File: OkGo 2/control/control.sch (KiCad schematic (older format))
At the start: 40 parts

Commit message: Removed RFM GPIOs, added control LCD, removed LEDs
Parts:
- removed P?: CONN_CH1, symbol CONN_01X05
- removed P?: CONN_CH2, symbol CONN_01X05
- removed P?: CONN_CH3, symbol CONN_01X05
- removed P?: CONN_CH4, symbol CONN_01X05
- removed R? (x8): R, symbol R
- added P?: CONN_CH1, symbol CONN_01X02
- added P?: CONN_CH2, symbol CONN_01X02
- added P?: CONN_CH3, symbol CONN_01X02
- added P?: CONN_CH4, symbol CONN_01X02
- added RV?: 20k LIN, symbol POT
- added U?: LCD_HD44780, symbol LCD_HD44780
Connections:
- net labels added: LCD_DB0, LCD_DB1, LCD_DB2, LCD_DB3, LCD_DB4, LCD_DB5, LCD_DB6, LCD_DB7, LCD_E, LCD_R/W, LCD_RS
- net labels removed: CH1_GRN, CH1_RED, CH2_GRN, CH2_RED, CH3_GRN, CH3_RED, CH4_GRN, CH4_RED, DIO0, DIO1, DIO2, DIO3, DIO4, DIO5
- wire segments 192 -> 170
- no-connect marks 2 -> 8
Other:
- moved on the sheet: C?, P?, R?, U?

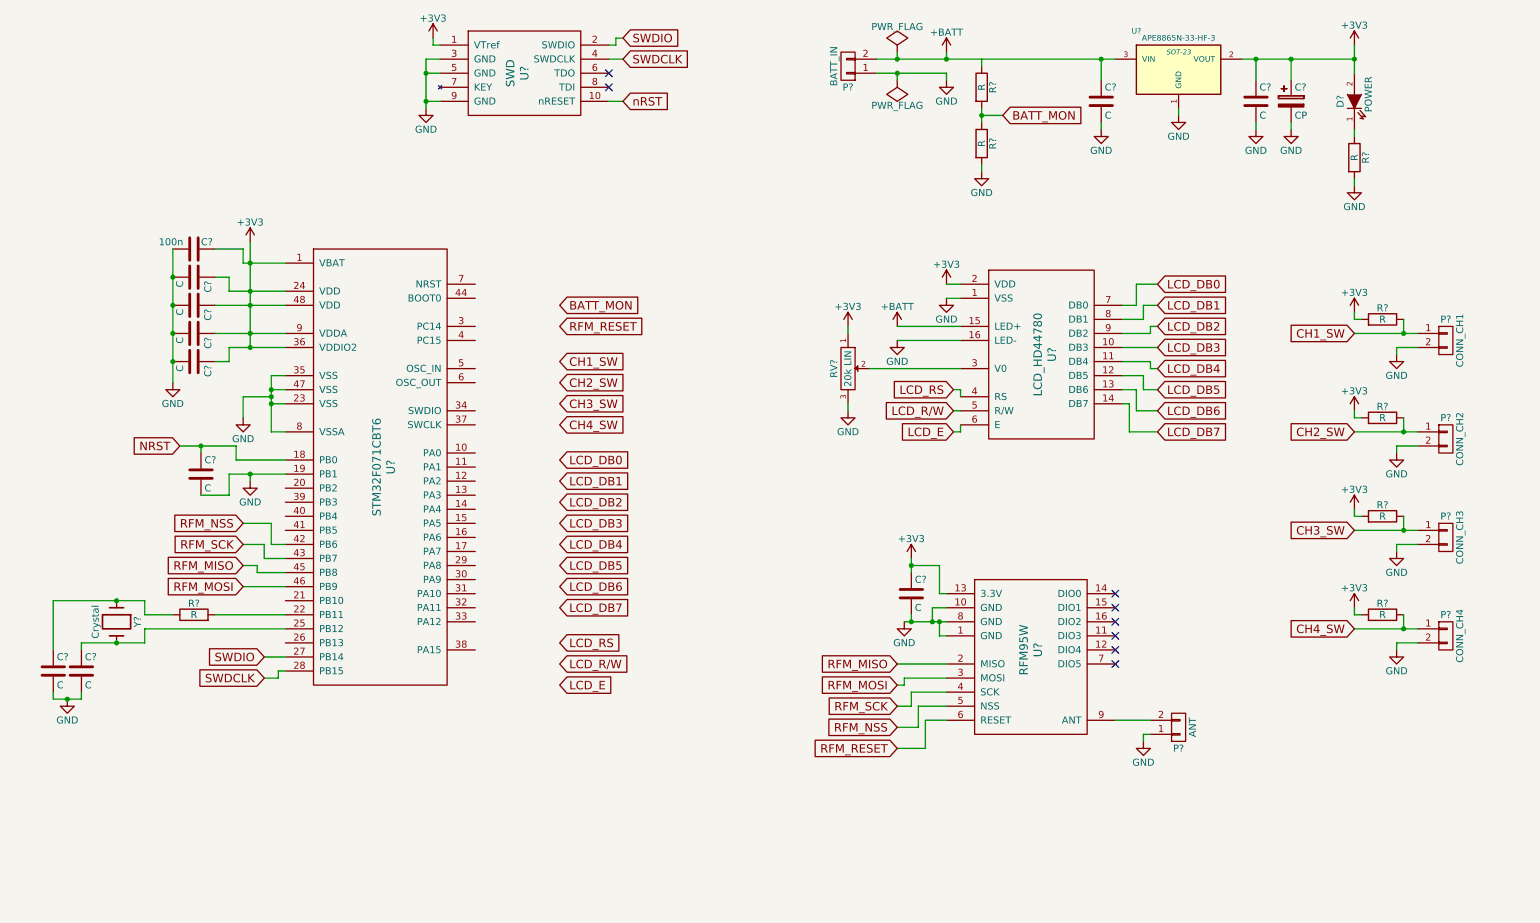
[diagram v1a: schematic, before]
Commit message: Updated schematics to new KiCAD
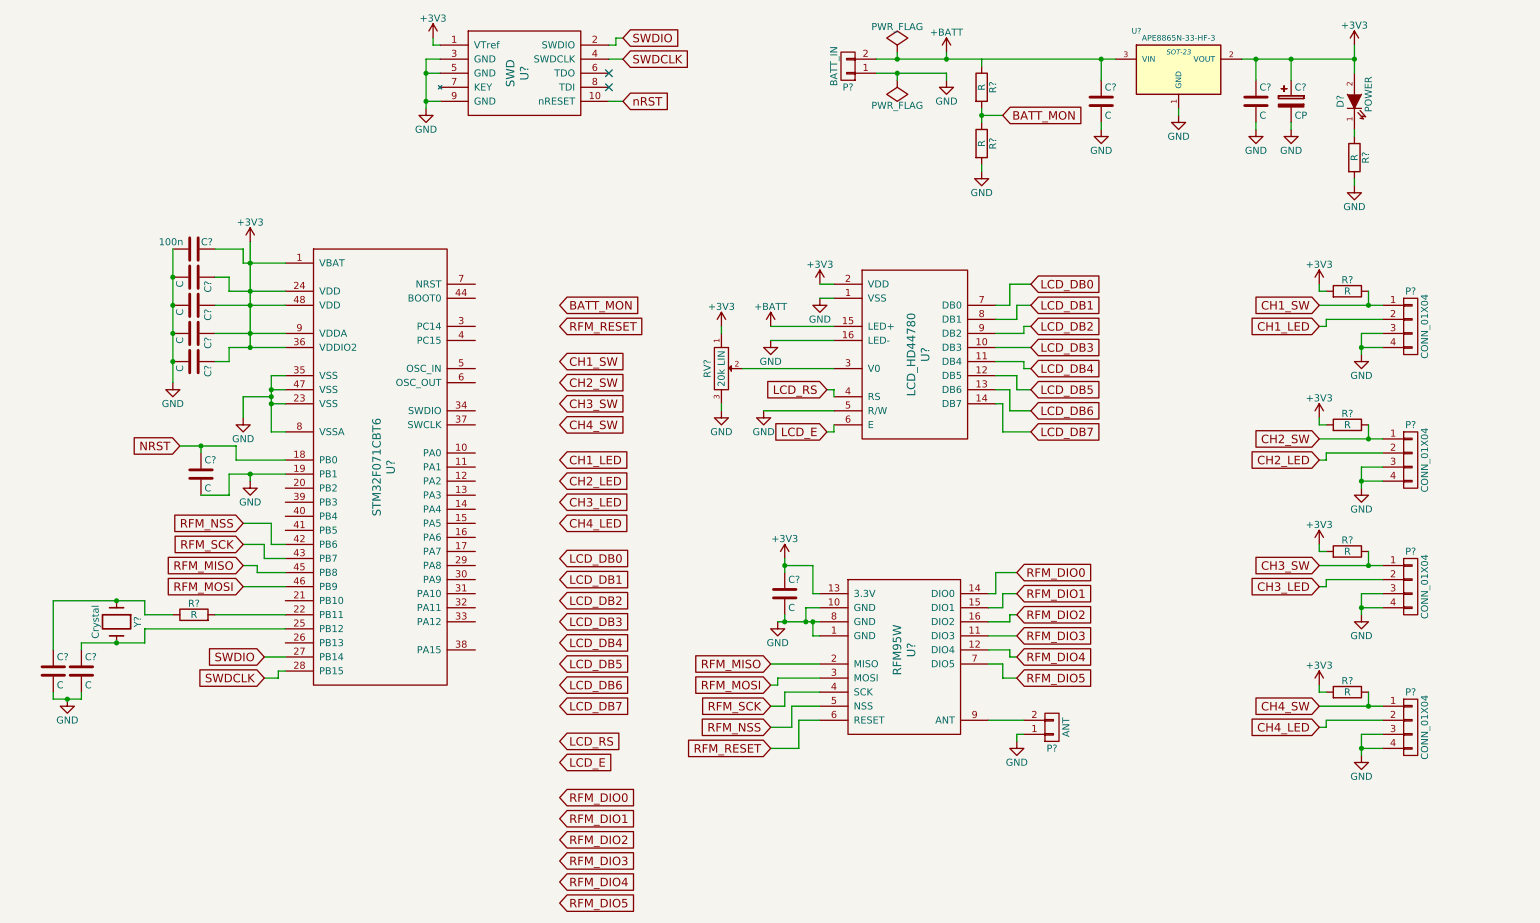
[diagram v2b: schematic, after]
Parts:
- removed P?: CONN_CH1, symbol CONN_01X02
- removed P?: CONN_CH2, symbol CONN_01X02
- removed P?: CONN_CH3, symbol CONN_01X02
- removed P?: CONN_CH4, symbol CONN_01X02
- added P? (x4): CONN_01X04, symbol CONN_01X04
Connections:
- net LCD_R/W is gone; now on net GND: U?.5 (R/W)
- net CH1_SW: now also P?.1 (P1)
- net CH2_SW: now also P?.1 (P1)
- net CH3_SW: now also P?.1 (P1)
- net CH4_SW: now also P?.1 (P1)
- net GND: now also P?.3 (P3), P?.3 (P3), P?.3 (P3), P?.3 (P3), P?.4 (P4), P?.4 (P4), P?.4 (P4), P?.4 (P4)
- net RFM_DIO3: now reaches U?.11 (DIO3)
- net RFM_DIO4: now reaches U?.12 (DIO4)
- net RFM_DIO0: now reaches U?.14 (DIO0)
- net RFM_DIO1: now reaches U?.15 (DIO1)
- net RFM_DIO2: now reaches U?.16 (DIO2)
- net RFM_DIO5: now reaches U?.7 (DIO5)
- new net CH1_LED: P?.2 (P2)
- new net CH2_LED: P?.2 (P2)
- new net CH3_LED: P?.2 (P2)
- new net CH4_LED: P?.2 (P2)
- no-connect marks 8 -> 2
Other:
- moved on the sheet: C?, P?, R?, RV?, U?

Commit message: Removed SPI pins from STM32 pinout.
Made them generic pins for more flexibility and less weirdness.  Resolves #1.
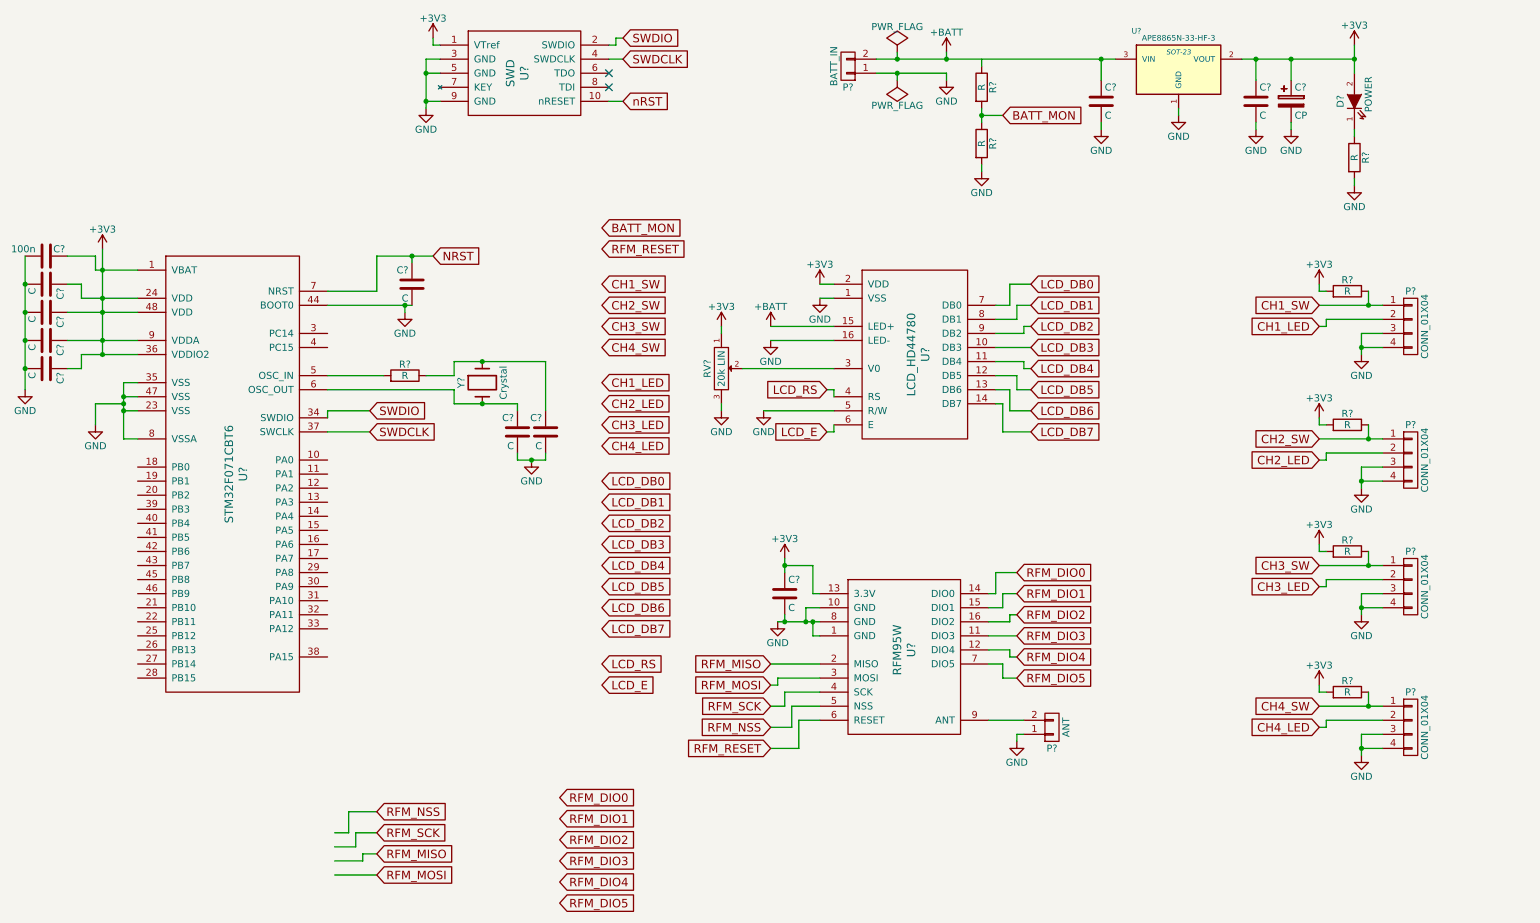
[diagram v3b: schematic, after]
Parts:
- removed U?: STM32F071CBT6, symbol STM32F071CBT6
- added U?: STM32F071CBT6, symbol STM32F071CBT6
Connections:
- net +3V3: now also U?.1 (VBAT), U?.24 (VDD), U?.36 (VDDIO2), U?.48 (VDD), U?.9 (VDDA)
- net GND: now also U?.23 (VSS), U?.35 (VSS), U?.44 (BOOT0), U?.47 (VSS), U?.8 (VSSA)
- net NRST: now also U?.7 (NRST)
- net SWDCLK: now also U?.37 (SWCLK)
- net SWDIO: now also U?.34 (SWDIO)
- net at R?.2: now also U?.5 (OSC_IN)
- net at C?.1, Y?.2: now also U?.6 (OSC_OUT)
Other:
- moved on the sheet: C?, R?, Y?

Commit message: Added ESD suppression, resolves #13
Also removed redundant pulldowns on firing channels.
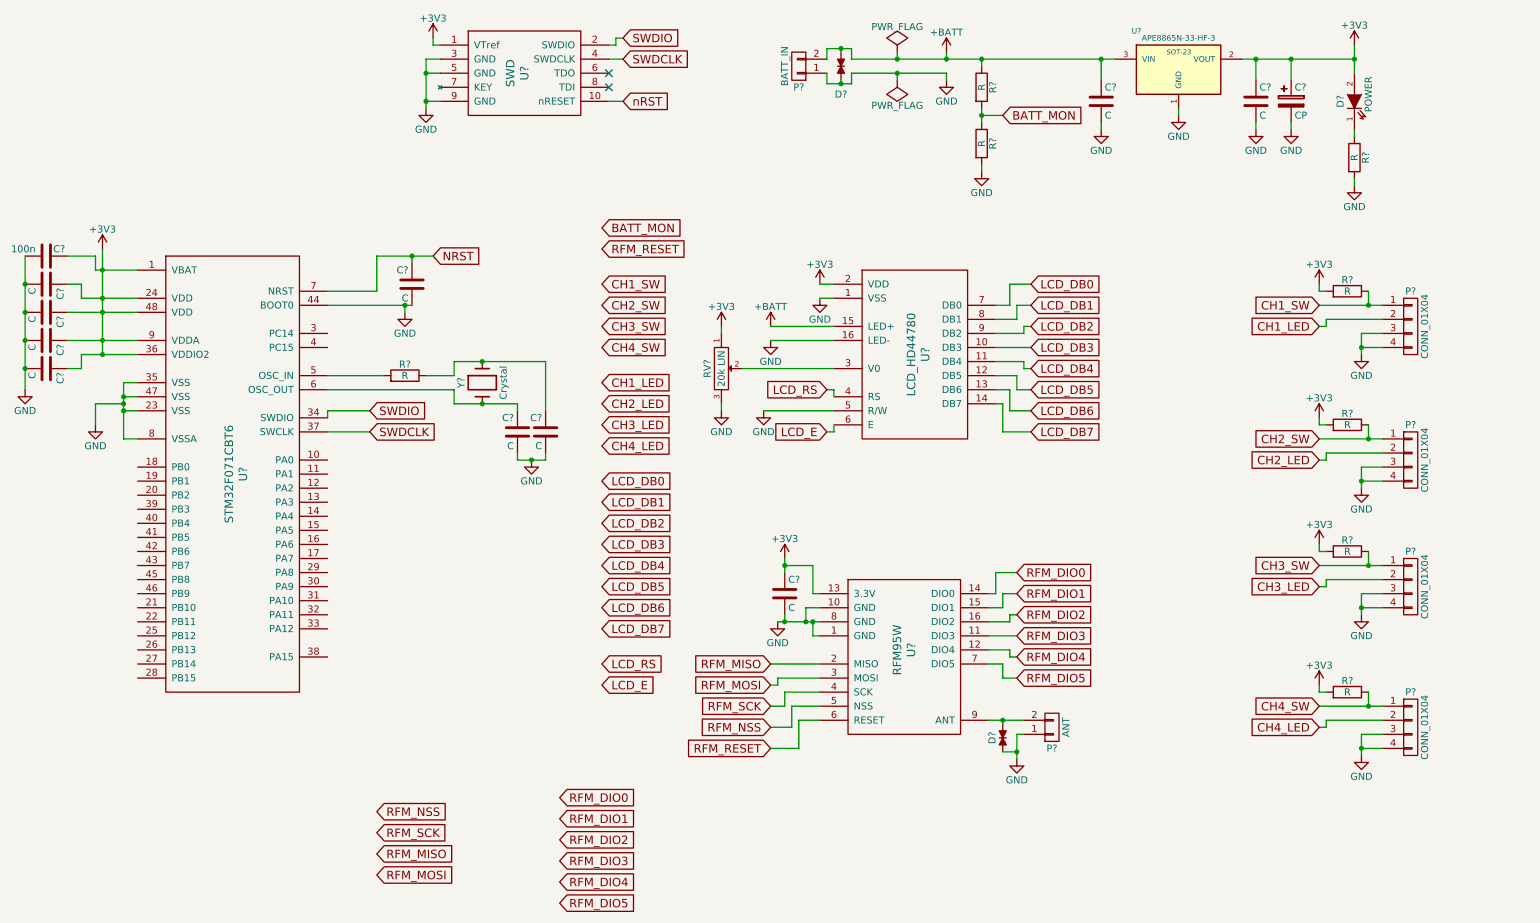
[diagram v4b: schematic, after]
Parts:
- added D? (x2): TVS_small, Resistors_SMD:R_0603_HandSoldering, symbol TVS_small
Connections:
- net +BATT: now also R?.1, D?.1
- net GND: now also D?.1, D?.2
- net at P?.2 (P2), U?.9 (ANT): now also D?.2
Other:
- moved on the sheet: P?
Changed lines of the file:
@@
 LIBS:lcd_hd44780
 LIBS:stm32f071cbt6
+LIBS:tvs_small
 LIBS:control-cache
 EELAYER 25 0
@@
 L CONN_01X02 P?
 U 1 1 556213DD
-P 6700 1150
-F 0 "P?" H 6700 1300 50  0000 C CNN
-F 1 "BATT_IN" V 6800 1150 50  0000 C CNN
-F 2 "" H 6700 1150 60  0000 C CNN
-F 3 "" H 6700 1150 60  0000 C CNN
-	1    6700 1150
+P 6350 1150
+F 0 "P?" H 6350 1300 50  0000 C CNN
+F 1 "BATT_IN" V 6450 1150 50  0000 C CNN
+F 2 "" H 6350 1150 60  0000 C CNN
+F 3 "" H 6350 1150 60  0000 C CNN
+	1    6350 1150
 	-1   0    0    1
 $EndComp
@@
 L GND #PWR?
 U 1 1 55629E65
-P 7900 5950
-F 0 "#PWR?" H 7900 5700 50  0001 C CNN
-F 1 "GND" H 7900 5800 50  0000 C CNN
-F 2 "" H 7900 5950 60  0000 C CNN
-F 3 "" H 7900 5950 60  0000 C CNN
-	1    7900 5950
+P 7900 6075
+F 0 "#PWR?" H 7900 5825 50  0001 C CNN
+F 1 "GND" H 7900 5925 50  0000 C CNN
+F 2 "" H 7900 6075 60  0000 C CNN
+F 3 "" H 7900 6075 60  0000 C CNN
+	1    7900 6075
 	1    0    0    -1
 $EndComp
@@
 	9850 1550 9850 1600
 Wire Wire Line
-	9500 1100 10300 1100
+	9500 1100 9600 1100
+Wire Wire Line
+	9600 1100 9850 1100
+Wire Wire Line
+	9850 1100 10300 1100
 Wire Wire Line
 	9600 1100 9600 1250
@@
 Connection ~ 9600 1100
 Wire Wire Line
-	10300 1000 10300 1200
+	10300 1000 10300 1100
+Wire Wire Line
+	10300 1100 10300 1200
 Connection ~ 9850 1100
 Wire Wire Line
-	6900 1200 7400 1200
+	6725 1200 7050 1200
+Wire Wire Line
+	7050 1200 7400 1200
 Wire Wire Line
 	7050 1050 7050 1100
@@
 	10350 3150 10500 3150
 Wire Wire Line
-	10350 3050 10350 3200
+	10350 3050 10350 3150
+Wire Wire Line
+	10350 3150 10350 3200
 Wire Wire Line
 	10350 4100 10500 4100
 Wire Wire Line
-	10350 4000 10350 4150
+	10350 4000 10350 4100
+Wire Wire Line
+	10350 4100 10350 4150
 Wire Wire Line
 	10350 5000 10500 5000
 Wire Wire Line
-	10350 4900 10350 5050
+	10350 4900 10350 5000
+Wire Wire Line
+	10350 5000 10350 5050
 Wire Wire Line
 	10350 6000 10500 6000
 Wire Wire Line
-	10350 5900 10350 6050
+	10350 5900 10350 6000
+Wire Wire Line
+	10350 6000 10350 6050
 Wire Wire Line
 	10400 2850 10400 2750
@@
 	10050 2750 10050 2700
 Wire Wire Line
-	10050 2850 10500 2850
-Wire Wire Line
-	10050 3800 10500 3800
+	10050 2850 10400 2850
+Wire Wire Line
+	10400 2850 10500 2850
+Wire Wire Line
+	10050 3800 10400 3800
+Wire Wire Line
+	10400 3800 10500 3800
 Wire Wire Line
 	10400 3800 10400 3700
@@
 	10050 3700 10050 3650
 Wire Wire Line
-	10050 4700 10500 4700
+	10050 4700 10400 4700
+Wire Wire Line
+	10400 4700 10500 4700
 Wire Wire Line
 	10100 4600 10050 4600
@@
 Connection ~ 10400 4700
 Wire Wire Line
-	10050 5700 10500 5700
+	10050 5700 10400 5700
+Wire Wire Line
+	10400 5700 10500 5700
 Wire Wire Line
 	10400 5600 10400 5700
@@
 	7950 5900 7900 5900
 Wire Wire Line
-	7900 5900 7900 5950
-Wire Wire Line
-	6200 5100 6500 5100
+	7900 5900 7900 6025
+Wire Wire Line
+	7900 6025 7900 6075
+Wire Wire Line
+	6200 5100 6250 5100
+Wire Wire Line
+	6250 5100 6400 5100
+Wire Wire Line
+	6400 5100 6450 5100
+Wire Wire Line
+	6450 5100 6500 5100
 Wire Wire Line
 	6450 5100 6450 5200
@@
 Connection ~ 6400 5100
 Wire Wire Line
-	6250 4650 6250 4750
+	6250 4650 6250 4700
+Wire Wire Line
+	6250 4700 6250 4750
 Wire Wire Line
 	6250 4700 6450 4700
@@
 Connection ~ 6250 5100
 Wire Wire Line
-	7950 5800 7700 5800
-Wire Wire Line
-	1400 2450 1400 3200
-Wire Wire Line
-	1250 2800 1650 2800
-Wire Wire Line
-	1150 2900 1650 2900
+	7950 5800 7800 5800
+Wire Wire Line
+	7800 5800 7700 5800
+Wire Wire Line
+	1400 2450 1400 2600
+Wire Wire Line
+	1400 2600 1400 2800
+Wire Wire Line
+	1400 2800 1400 2900
+Wire Wire Line
+	1400 2900 1400 3100
+Wire Wire Line
+	1400 3100 1400 3200
+Wire Wire Line
+	1250 2800 1400 2800
+Wire Wire Line
+	1400 2800 1650 2800
+Wire Wire Line
+	1150 2900 1400 2900
+Wire Wire Line
+	1400 2900 1650 2900
 Connection ~ 1400 2800
 Wire Wire Line
-	1150 3100 1650 3100
+	1150 3100 1400 3100
+Wire Wire Line
+	1400 3100 1650 3100
 Connection ~ 1400 2900
 Wire Wire Line
-	1250 3200 1650 3200
+	1250 3200 1400 3200
+Wire Wire Line
+	1400 3200 1650 3200
 Connection ~ 1400 3100
 Connection ~ 1400 3200
@@
 	1650 3400 1550 3400
 Wire Wire Line
-	1550 3400 1550 3800
+	1550 3400 1550 3500
+Wire Wire Line
+	1550 3500 1550 3550
+Wire Wire Line
+	1550 3550 1550 3600
+Wire Wire Line
+	1550 3600 1550 3800
 Wire Wire Line
 	1550 3500 1650 3500
@@
 Connection ~ 3600 2500
 Wire Wire Line
-	3000 2850 3600 2850
+	3000 2850 3550 2850
+Wire Wire Line
+	3550 2850 3600 2850
 Wire Wire Line
 	3550 2850 3550 2900
 Wire Wire Line
-	3750 2500 3350 2500
+	3350 2500 3600 2500
+Wire Wire Line
+	3600 2500 3750 2500
 Wire Wire Line
 	3350 2750 3000 2750
 Wire Wire Line
-	3350 6450 3150 6450
-Wire Wire Line
-	3150 6450 3150 6600
-Wire Wire Line
-	3150 6600 3050 6600
-Wire Wire Line
-	3350 6600 3200 6600
-Wire Wire Line
-	3200 6600 3200 6700
-Wire Wire Line
-	3200 6700 3050 6700
-Wire Wire Line
-	3350 6900 3050 6900
-Wire Wire Line
-	3350 6750 3250 6750
-Wire Wire Line
-	3250 6750 3250 6800
-Wire Wire Line
-	3250 6800 3050 6800
-Wire Wire Line
 	3000 3750 3300 3750
 Wire Wire Line
@@
 	3900 3350 3900 3250
 Wire Wire Line
-	3900 3250 4550 3250
+	3900 3250 4100 3250
+Wire Wire Line
+	4100 3250 4550 3250
 Wire Wire Line
 	3900 3450 3900 3550
 Wire Wire Line
-	3900 3550 4350 3550
+	3900 3550 4100 3550
+Wire Wire Line
+	4100 3550 4350 3550
 Wire Wire Line
 	4350 3550 4350 3600
@@
 Connection ~ 4100 3250
 Wire Wire Line
-	4550 3900 4550 3950
-Wire Wire Line
-	4550 3950 4350 3950
+	4550 3950 4550 3900
+Wire Wire Line
+	4350 3950 4450 3950
+Wire Wire Line
+	4450 3950 4550 3950
 Connection ~ 4450 3950
 Wire Wire Line
@@
 	1250 3300 1150 3300
 Wire Wire Line
-	850  2500 850  3450
+	850  2500 850  2700
+Wire Wire Line
+	850  2700 850  2900
+Wire Wire Line
+	850  2900 850  3100
+Wire Wire Line
+	850  3100 850  3300
+Wire Wire Line
+	850  3300 850  3450
 Connection ~ 850  2900
 Connection ~ 850  3100
@@
 	3800 1100 3700 1100
 Wire Wire Line
-	3700 1100 3700 1450
+	3700 1100 3700 1200
+Wire Wire Line
+	3700 1200 3700 1400
+Wire Wire Line
+	3700 1400 3700 1450
 Wire Wire Line
 	3700 1400 3800 1400
@@
 	1350 2500 1350 2600
 Wire Wire Line
-	1350 2600 1650 2600
+	1350 2600 1400 2600
+Wire Wire Line
+	1400 2600 1650 2600
 Connection ~ 1400 2600
 Connection ~ 850  2700
@@
 	7650 1850 7650 1900
 Wire Wire Line
-	7650 1450 7650 1550
+	7650 1450 7650 1500
+Wire Wire Line
+	7650 1500 7650 1550
 Wire Wire Line
 	7650 1500 7800 1500
@@
 BATT_MON
 Wire Wire Line
-	6900 1100 8600 1100
+	6725 1100 7050 1100
+Wire Wire Line
+	7050 1100 7400 1100
+Wire Wire Line
+	7400 1100 7650 1100
+Wire Wire Line
+	7650 1100 8500 1100
+Wire Wire Line
+	8500 1100 8600 1100
 Text GLabel 4950 2300 2    60   Input ~ 0
 BATT_MON
@@
 Wire Wire Line
 	3000 3650 3000 3600
+$Comp
+L TVS_small D?
+U 1 1 559DC9F3
+P 6650 1150
+F 0 "D?" V 6850 1150 50  0000 C CNN
+F 1 "TVS_small" H 6650 1075 50  0001 C CNN
+F 2 "Resistors_SMD:R_0603_HandSoldering" H 6650 1150 60  0001 C CNN
+F 3 "" H 6650 1150 60  0000 C CNN
+F 4 "2368174" H 6650 1150 60  0001 C CNN "Farnell"
+	1    6650 1150
+	0    1    1    0
+$EndComp
+Wire Wire Line
+	6550 1100 6550 1025
+Wire Wire Line
+	6550 1025 6650 1025
+Wire Wire Line
+	6650 1025 6725 1025
+Wire Wire Line
+	6650 1025 6650 1050
+Wire Wire Line
+	6725 1025 6725 1100
+Connection ~ 6650 1025
+Wire Wire Line
+	6550 1200 6550 1275
+Wire Wire Line
+	6550 1275 6650 1275
+Wire Wire Line
+	6650 1275 6725 1275
+Wire Wire Line
+	6650 1275 6650 1250
+Wire Wire Line
+	6725 1275 6725 1200
+Connection ~ 6650 1275
+Connection ~ 7650 1100
+$Comp
+L TVS_small D?
+U 1 1 559DD518
+P 7800 5925
+F 0 "D?" H 7800 6000 50  0000 C CNN
+F 1 "TVS_small" H 7800 5850 50  0001 C CNN
+F 2 "Resistors_SMD:R_0603_HandSoldering" H 7800 5925 60  0001 C CNN
+F 3 "" H 7800 5925 60  0000 C CNN
+F 4 "2368174" H 7800 5925 60  0001 C CNN "Farnell"
+	1    7800 5925
+	0    -1   -1   0
+$EndComp
+Wire Wire Line
+	7800 5800 7800 5825
+Connection ~ 7800 5800
+Wire Wire Line
+	7800 6025 7900 6025
+Connection ~ 7900 6025
 $EndSCHEMATC
